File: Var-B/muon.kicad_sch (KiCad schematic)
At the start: 9 parts, among them J1 HRO_TYPE-C-31-M-12, J2 SM04B-SRSS-TB, U1 TPD4E05U06DQA

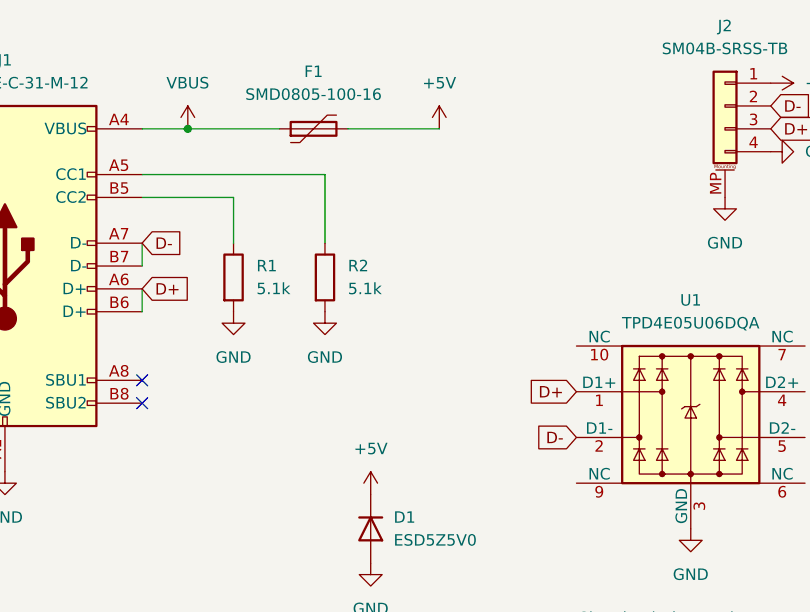
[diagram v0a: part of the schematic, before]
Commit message: Update B variant to B2
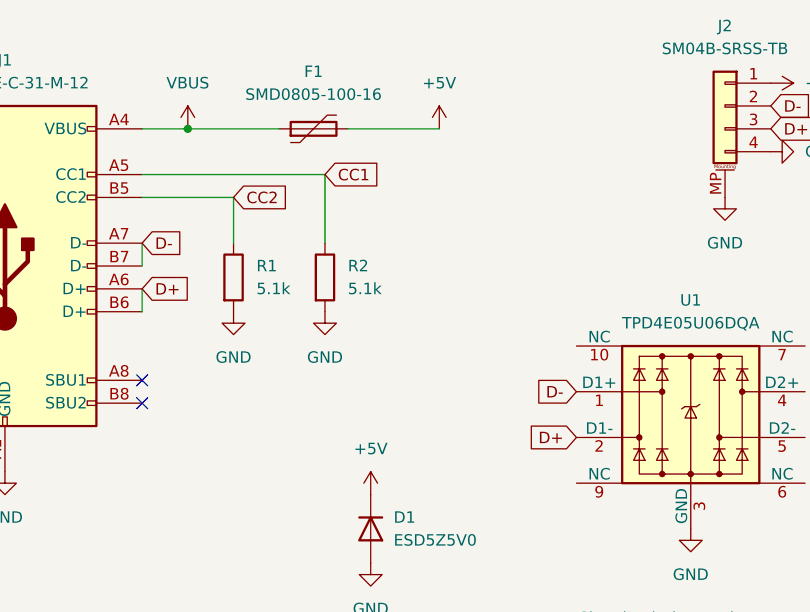
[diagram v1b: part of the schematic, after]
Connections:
- net D+: now also U1.2 (D1-); no longer U1.1 (D1+)
- net D-: now also U1.1 (D1+); no longer U1.2 (D1-)
- net CC1: now reaches J1.A5 (CC1), R2.1
- net CC2: now reaches J1.B5 (CC2), R1.1
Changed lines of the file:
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@@
+		)
+	)
+	(global_label "CC2"
+		(shape input)
+		(at 86.36 60.96 0)
+		(fields_autoplaced yes)
+		(effects
+			(font
+				(size 1.27 1.27)
+			)
+			(justify left)
+		)
+		(property "Intersheetrefs" "${INTERSHEET_REFS}"
+			(at 93.0947 60.96 0)
+			(effects
+				(font
+					(size 1.27 1.27)
+				)
+				(justify left)
+				(hide yes)
+			)
 		)
 	)
@@
 	(global_label "D+"
 		(shape input)
-		(at 124.46 82.55 180)
+		(at 124.46 87.63 180)
 		(fields_autoplaced yes)
 		(effects
@@
 		)
 		(property "Intersheetrefs" "${INTERSHEET_REFS}"
-			(at 118.6324 82.55 0)
+			(at 118.6324 87.63 0)
 			(effects
 				(font
@@
 	(global_label "D-"
 		(shape input)
-		(at 124.46 87.63 180)
+		(at 124.46 82.55 180)
 		(fields_autoplaced yes)
 		(effects
@@
 		)
 		(property "Intersheetrefs" "${INTERSHEET_REFS}"
-			(at 118.6324 87.63 0)
+			(at 118.6324 82.55 0)
 			(effects
 				(font
@@
 			(effects
 				(font
+					(size 1.27 1.27)
+				)
+				(justify left)
+				(hide yes)
+			)
+		)
+	)
+	(global_label "CC1"
+		(shape input)
+		(at 96.52 58.42 0)
+		(fields_autoplaced yes)
+		(effects
+			(font
+				(size 1.27 1.27)
+			)
+			(justify left)
+		)
+		(property "Intersheetrefs" "${INTERSHEET_REFS}"
+			(at 103.2547 58.42 0)
+			(effects
+				(font
